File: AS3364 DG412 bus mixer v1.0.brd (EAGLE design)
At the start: 81.3 x 36.8 mm, 151 parts, among them IC1 PCA9539PW, IC10 DG412-J, IC11 DG412-J, IC14 TL074JT, IC2 TL074JT, IC3 TL072JT, IC4 TL074JT, IC6 TL072JT, IC8 DG412-J, IC9 DG412-J

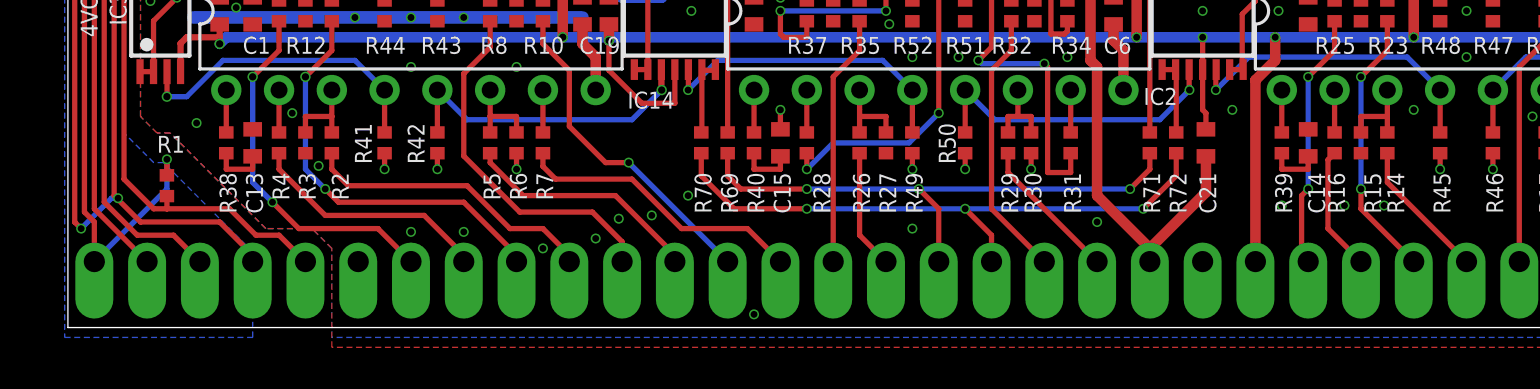
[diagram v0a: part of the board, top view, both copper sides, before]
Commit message: Replaced connectors
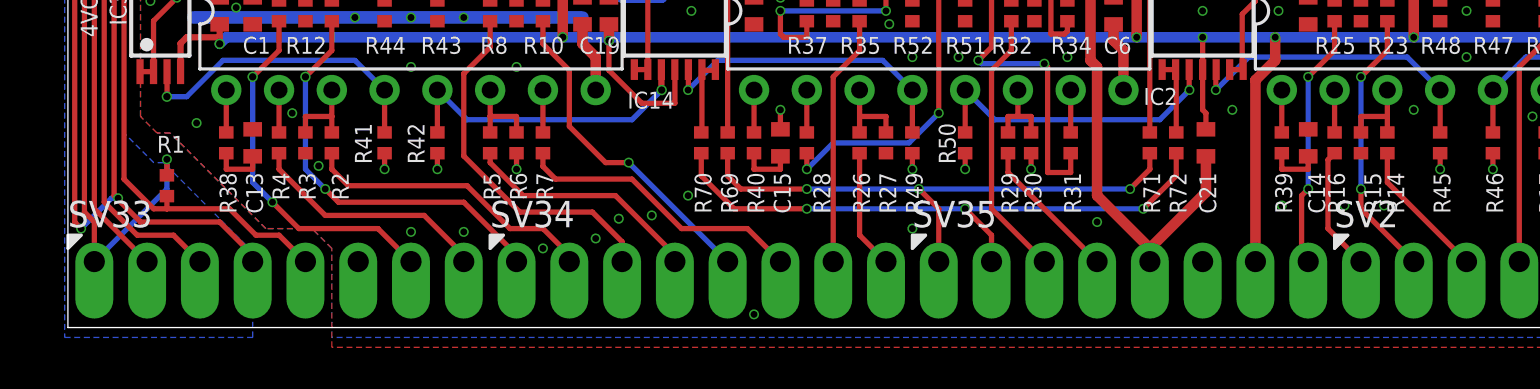
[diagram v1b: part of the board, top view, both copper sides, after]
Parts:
- removed SV1, SV10, SV11, SV12, SV13, SV14, SV15, SV16, SV17, SV18, SV19, SV20, SV21, SV22, SV23, SV24, SV25, SV26, SV27, SV28, SV29, SV3, SV30, SV31, SV32, SV4, SV5, SV6, SV7, SV8, SV9: (no value), joakim:SIP-PIN01-1J
- added SV33, SV34, SV35: (no value), joakim:SIP-PIN08-1J
- SV2: device joakim:SIP-PIN01-1J -> joakim:SIP-PIN08-1J
- moved SV2 69.9 mm to (71.1, 3.17)
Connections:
- net !RST: now also SV33.5; no longer SV6.1
- net +12V: now also SV35.5; no longer SV21.1
- net +3V3: now also SV33.1; no longer SV2.1
- net -12V: now also SV35.7; no longer SV31.1
- net CV1: now also SV34.1; no longer SV11.1
- net CV2: now also SV34.2; no longer SV12.1
- net CV3: now also SV34.3; no longer SV13.1
- net CV4: now also SV34.4; no longer SV14.1
- net CV5: now also SV2.2; no longer SV27.1
- net CV6: now also SV2.3; no longer SV28.1
- net CV7: now also SV2.4; no longer SV29.1
- net CV8: now also SV2.5; no longer SV30.1
- net CV_A_DRY: now also SV34.7; no longer SV15.1
- net CV_A_WET: now also SV35.3; no longer SV16.1
- net CV_B_DRY: now also SV34.8; no longer SV17.1
- net CV_B_WET: now also SV35.4; no longer SV18.1
- net DGND: now also SV33.4; no longer SV5.1
- net GND: now also SV35.6; no longer SV22.1
- net IN1: now also SV33.7; no longer SV7.1
- net IN2: now also SV33.8; no longer SV8.1
- net IN3: now also SV34.5; no longer SV9.1
- net IN4: now also SV34.6; no longer SV10.1
- net IN5: now also SV35.8; no longer SV23.1
- net IN6: now also SV2.1; no longer SV24.1
- net IN7: now also SV2.6; no longer SV25.1
- net IN8: now also SV2.7; no longer SV26.1
- net LPF_IN_100K_MIX: now also SV35.2; no longer SV20.1
- net SCL: now also SV33.3; no longer SV4.1
- net SDA: now also SV33.2; no longer SV3.1
- net SVF_IN_100K_MIX: now also SV35.1; no longer SV19.1

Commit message: Added sum a and b to output pins
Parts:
- moved R26 1.27 mm to (39.4, 8.89)
- moved R27 1.27 mm to (38.1, 8.89)
- moved C21 0.16 mm to (54.6, 8.89)
- renumbered SV2 to SV3, SV34 to SV1, SV35 to SV4
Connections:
- removed net LPF_IN_100K_MIX: R70.2, R72.2, SV4.2
- removed net SVF_IN_100K_MIX: R69.2, R71.2, SV4.1
- new net OUT_A_100K_MIX: R69.2, R71.2, SV4.2
- new net OUT_B_100K_MIX: R70.2, R72.2, SV4.3
- net +12V: now also SV4.6; no longer SV4.5
- net -12V: now also SV4.8; no longer SV4.7
- net CV1: now also SV33.8; no longer SV1.1
- net CV2: now also SV1.1; no longer SV1.2
- net CV3: now also SV1.2; no longer SV1.3
- net CV4: now also SV1.3; no longer SV1.4
- net CV5: now also SV3.3; no longer SV3.2
- net CV6: now also SV3.4; no longer SV3.3
- net CV7: now also SV3.5; no longer SV3.4
- net CV8: now also SV3.6; no longer SV3.5
- net CV_A_DRY: now also SV1.8; no longer SV1.7
- net CV_A_WET: now also SV4.4; no longer SV4.3
- net CV_B_DRY: now also SV4.1; no longer SV1.8
- net CV_B_WET: now also SV4.5; no longer SV4.4
- net GND: now also SV4.7; no longer SV4.6
- net IN1: now also SV33.6; no longer SV33.7
- net IN2: now also SV33.7; no longer SV33.8
- net IN3: now also SV1.4; no longer SV1.5
- net IN4: now also SV1.5; no longer SV1.6
- net IN5: now also SV3.1; no longer SV4.8
- net IN6: now also SV3.2; no longer SV3.1
- net IN7: now also SV3.7; no longer SV3.6
- net IN8: now also SV3.8; no longer SV3.7
- net SUM_A: now also SV1.6
- net SUM_B: now also SV1.7
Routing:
- net OUT_B_100K_MIX: track 0.00 -> 29.7 mm, vias 0 -> 3
- net LPF_IN_100K_MIX: track 29.4 -> 0.00 mm, vias 3 -> 0
- net SVF_IN_100K_MIX: track 26.7 -> 0.00 mm, vias 3 -> 0
- net OUT_A_100K_MIX: track 0.00 -> 26.5 mm, vias 0 -> 3
- net SUM_A: track 23.5 -> 34.4 mm, vias 4 -> 6
- net SUM_B: track 31.7 -> 36.6 mm
- net IN2: track 11.7 -> 8.96 mm
- net CV1: track 19.8 -> 17.1 mm
- net IN4: track 14.0 -> 11.4 mm
- net CV3: track 17.3 -> 14.8 mm
- net CV_B_WET: track 6.99 -> 9.34 mm
- net IN1: track 17.5 -> 15.1 mm
- net CV4: track 11.5 -> 9.24 mm
- net CV6: track 6.79 -> 8.88 mm
- net IN8: track 6.79 -> 8.87 mm
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
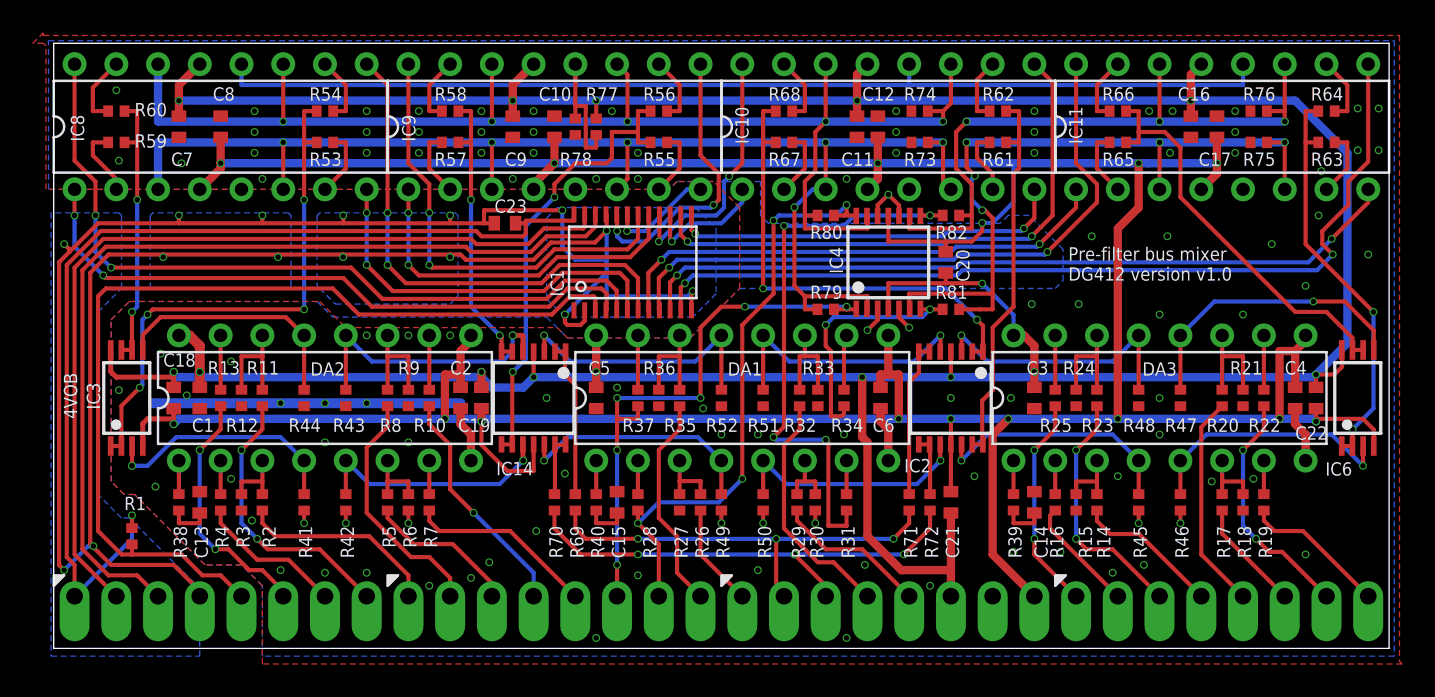
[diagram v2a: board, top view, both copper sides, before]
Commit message: New version with inverted vcas on inputs
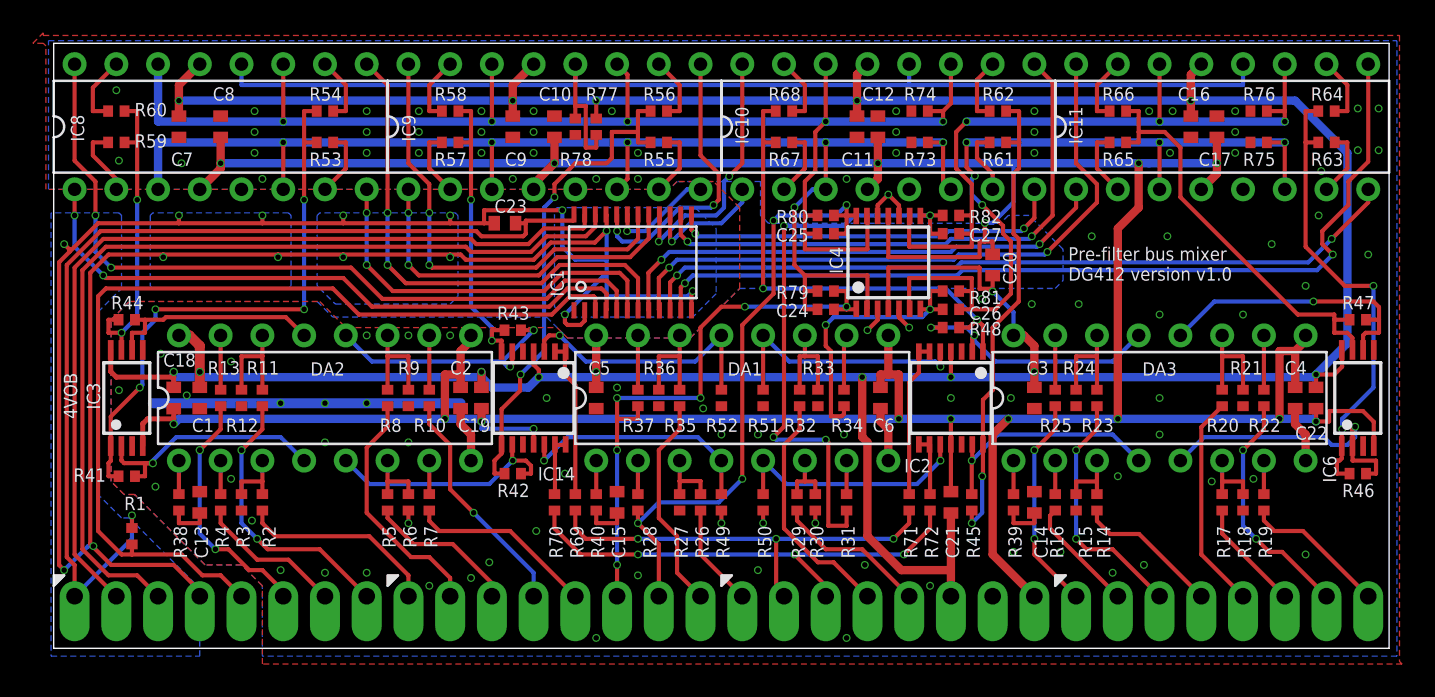
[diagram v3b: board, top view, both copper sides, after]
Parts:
- added C24, C25, C26, C27: 33pF, joakim:R0402
- moved R48 12.2 mm to (54.6, 19.5), turned to 180 degrees
- moved R47 11.8 mm to (79.4, 20.0), turned to 0 degrees
- moved R44 11.8 mm to (4.45, 20.0), turned to 0 degrees
- moved R43 11.0 mm to (27.9, 19.4), turned to 0 degrees
- moved R46 10.9 mm to (79.4, 10.6), turned to 0 degrees
- moved R41 10.9 mm to (4.45, 10.5), turned to 0 degrees
- moved R42 10.3 mm to (27.9, 10.6), turned to 0 degrees
- moved R45 10.2 mm to (55.9, 8.89)
- moved C20 2.86 mm to (57.1, 23.3)
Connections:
- net BUS_A: now also C24.1
- net BUS_B: now also C25.1
- net BUS_FX_A: now also C26.1
- net BUS_FX_B: now also C27.1
- net CON1: now also IC3.6; no longer IC3.5
- net CON2: now also IC3.2; no longer IC3.3
- net CON3: now also IC14.6; no longer IC14.5
- net CON4: now also IC14.9; no longer IC14.10
- net CON5: now also IC2.2; no longer IC2.3
- net CON6: now also IC2.13; no longer IC2.12
- net CON7: now also IC6.6; no longer IC6.5
- net CON8: now also IC6.2; no longer IC6.3
- net GND: now also IC14.10, IC14.5, IC2.12, IC2.3, IC3.3, IC3.5, IC6.3, IC6.5; no longer R41.1, R42.1, R43.1, R44.1, R45.1, R46.1, R47.1, R48.1
- net OUT1: now also R44.1; no longer IC3.6
- net OUT2: now also R41.1; no longer IC3.2
- net OUT3: now also R43.1; no longer IC14.6
- net OUT4: now also R42.1; no longer IC14.9
- net OUT5: now also R48.1; no longer IC2.2
- net OUT6: now also R45.1; no longer IC2.13
- net OUT7: now also R47.1; no longer IC6.6
- net OUT8: now also R46.1; no longer IC6.2
- net SUM_A: now also C24.2
- net SUM_B: now also C25.2
- net SUM_FX_A: now also C26.2
- net SUM_FX_B: now also C27.2
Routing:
- net OUT6: track 23.5 -> 28.9 mm, vias 0 -> 2
- net BUS_B: track 82.5 -> 85.8 mm
- net OUT8: track 24.8 -> 28.1 mm
- net BUS_FX_A: track 45.3 -> 48.6 mm
- net GND: track 41.2 -> 38.1 mm, vias 111 -> 107
- net BUS_FX_B: track 40.0 -> 43.0 mm
- net +12V: track 231.5 -> 234.2 mm
- net OUT4: track 28.3 -> 30.5 mm
- net BUS_A: track 80.5 -> 82.5 mm
- net OUT2: track 32.6 -> 34.6 mm
- net SUM_FX_A: track 15.1 -> 17.0 mm
- net SUM_FX_B: track 34.2 -> 36.1 mm
- net SUM_B: track 36.6 -> 38.4 mm
- net OUT1: track 16.9 -> 18.7 mm
- net SUM_A: track 34.4 -> 36.1 mm
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
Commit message: Fixed pin labeling
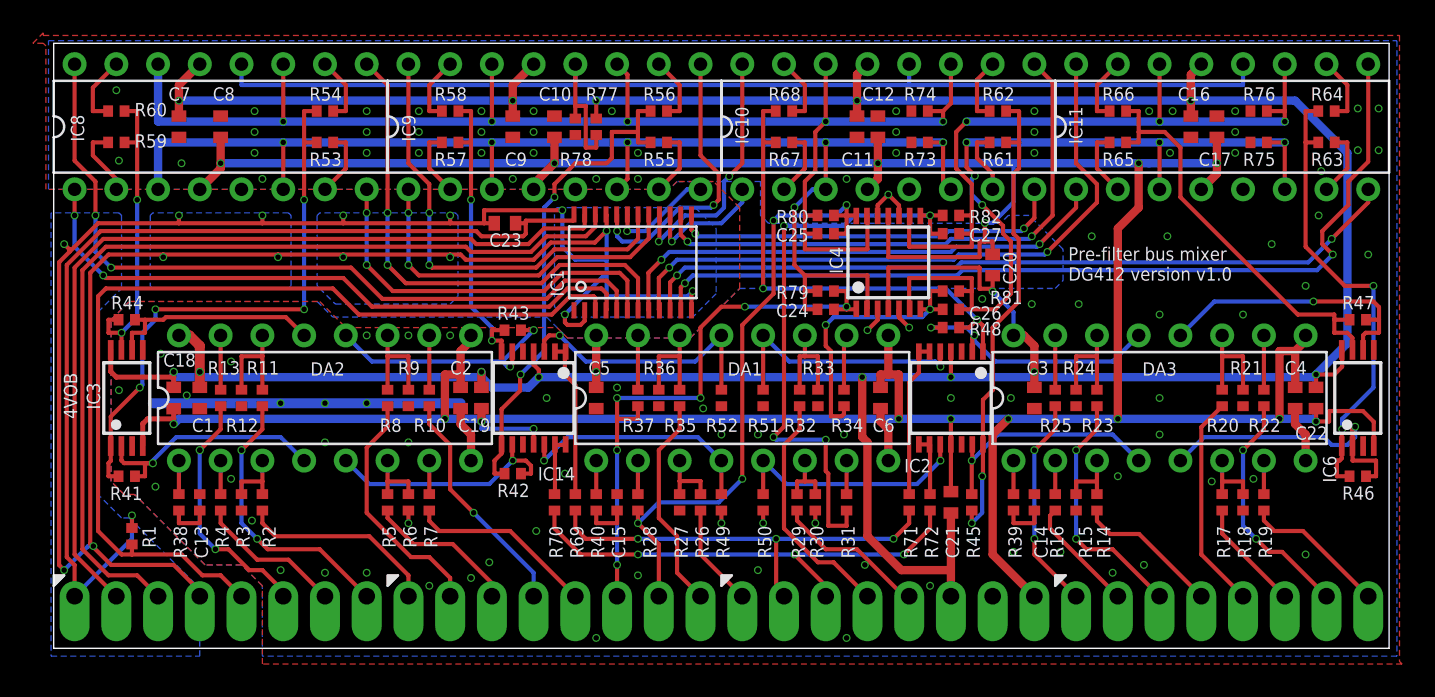
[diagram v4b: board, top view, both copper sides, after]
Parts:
- C13, C14, C15: device rcl:C0402 -> joakim:R0402
- moved R46 0.16 mm to (79.4, 10.5)
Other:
- board text added: "SUM A"
- board text added: "SUM B"
